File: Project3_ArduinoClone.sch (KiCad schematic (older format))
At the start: 0 parts

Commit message: Added list of parts. Added project symbols, except ATMEGA328. Added child sheet with connectors.
 Changes to be committed:
	new file:   Connectors.sch
	new file:   Portatil/Project3_ArduinoClone-roigmonzon-HP-Pavilion-dv7.pro
	new file:   Portatil/Project3_ArduinoClone-roigmonzon-HP-Pavilion-dv7.sch
	new file:   Project 3 parts.txt
	modified:   Project3_ArduinoClone-cache.lib
	modified:   Project3_ArduinoClone.sch
	modified:   Project3_ArduinoClone.sch-bak
	new file:   instrucciones git.txt
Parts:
- added BT?: Battery, symbol Device:Battery
- added C? (x2): C, symbol Device:C
- added C?: CP, symbol Device:CP
- added D?: LED, symbol Device:LED
- added R? (x2): R, symbol Device:R
- added U?: 24LC1025, symbol Memory_EEPROM:24LC1025
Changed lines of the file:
@@
 EESchema Schematic File Version 4
+LIBS:Project3_ArduinoClone-cache
 EELAYER 30 0
 EELAYER END
 $Descr A4 11693 8268
 encoding utf-8
-Sheet 1 1
+Sheet 1 2
 Title "Arduino Clone"
 Date "2019-10-12"
@@
 Comment4 ""
 $EndDescr
+$Comp
+L Device:Battery BT?
+U 1 1 5DA2ED42
+P 3550 2725
+F 0 "BT?" H 3658 2771 50  0000 L CNN
+F 1 "Battery" H 3658 2680 50  0000 L CNN
+F 2 "" V 3550 2785 50  0001 C CNN
+F 3 "~" V 3550 2785 50  0001 C CNN
+	1    3550 2725
+	1    0    0    -1
+$EndComp
+$Comp
+L Device:C C?
+U 1 1 5DA2FE65
+P 4125 2600
+F 0 "C?" H 4240 2646 50  0000 L CNN
+F 1 "C" H 4240 2555 50  0000 L CNN
+F 2 "" H 4163 2450 50  0001 C CNN
+F 3 "~" H 4125 2600 50  0001 C CNN
+	1    4125 2600
+	1    0    0    -1
+$EndComp
+$Comp
+L Device:C C?
+U 1 1 5DA30297
+P 4125 3075
+F 0 "C?" H 4240 3121 50  0000 L CNN
+F 1 "C" H 4240 3030 50  0000 L CNN
+F 2 "" H 4163 2925 50  0001 C CNN
+F 3 "~" H 4125 3075 50  0001 C CNN
+	1    4125 3075
+	1    0    0    -1
+$EndComp
+$Comp
+L Device:CP C?
+U 1 1 5DA309D4
+P 4125 3650
+F 0 "C?" H 4243 3696 50  0000 L CNN
+F 1 "CP" H 4243 3605 50  0000 L CNN
+F 2 "" H 4163 3500 50  0001 C CNN
+F 3 "~" H 4125 3650 50  0001 C CNN
+	1    4125 3650
+	1    0    0    -1
+$EndComp
+$Comp
+L Device:LED D?
+U 1 1 5DA313E3
+P 3475 3600
+F 0 "D?" H 3468 3816 50  0000 C CNN
+F 1 "LED" H 3468 3725 50  0000 C CNN
+F 2 "" H 3475 3600 50  0001 C CNN
+F 3 "~" H 3475 3600 50  0001 C CNN
+	1    3475 3600
+	1    0    0    -1
+$EndComp
+$Comp
+L Device:R R?
+U 1 1 5DA31FF8
+P 5100 2600
+F 0 "R?" H 5170 2646 50  0000 L CNN
+F 1 "R" H 5170 2555 50  0000 L CNN
+F 2 "" V 5030 2600 50  0001 C CNN
+F 3 "~" H 5100 2600 50  0001 C CNN
+	1    5100 2600
+	1    0    0    -1
+$EndComp
+$Comp
+L Device:R R?
+U 1 1 5DA326D9
+P 5100 3200
+F 0 "R?" H 5170 3246 50  0000 L CNN
+F 1 "R" H 5170 3155 50  0000 L CNN
+F 2 "" V 5030 3200 50  0001 C CNN
+F 3 "~" H 5100 3200 50  0001 C CNN
+	1    5100 3200
+	1    0    0    -1
+$EndComp
+$Comp
+L Memory_EEPROM:24LC1025 U?
+U 1 1 5DA32AA2
+P 6825 2950
+F 0 "U?" H 6825 3431 50  0000 C CNN
+F 1 "24LC1025" H 6825 3340 50  0000 C CNN
+F 2 "" H 6825 2950 50  0001 C CNN
+F 3 "http://ww1.microchip.com/downloads/en/DeviceDoc/21941B.pdf" H 6825 2950 50  0001 C CNN
+	1    6825 2950
+	1    0    0    -1
+$EndComp
+$Sheet
+S 6475 3875 1125 1900
+U 5DA33D85
+F0 "Connectors" 50
+F1 "Connectors.sch" 50
+$EndSheet
 $EndSCHEMATC

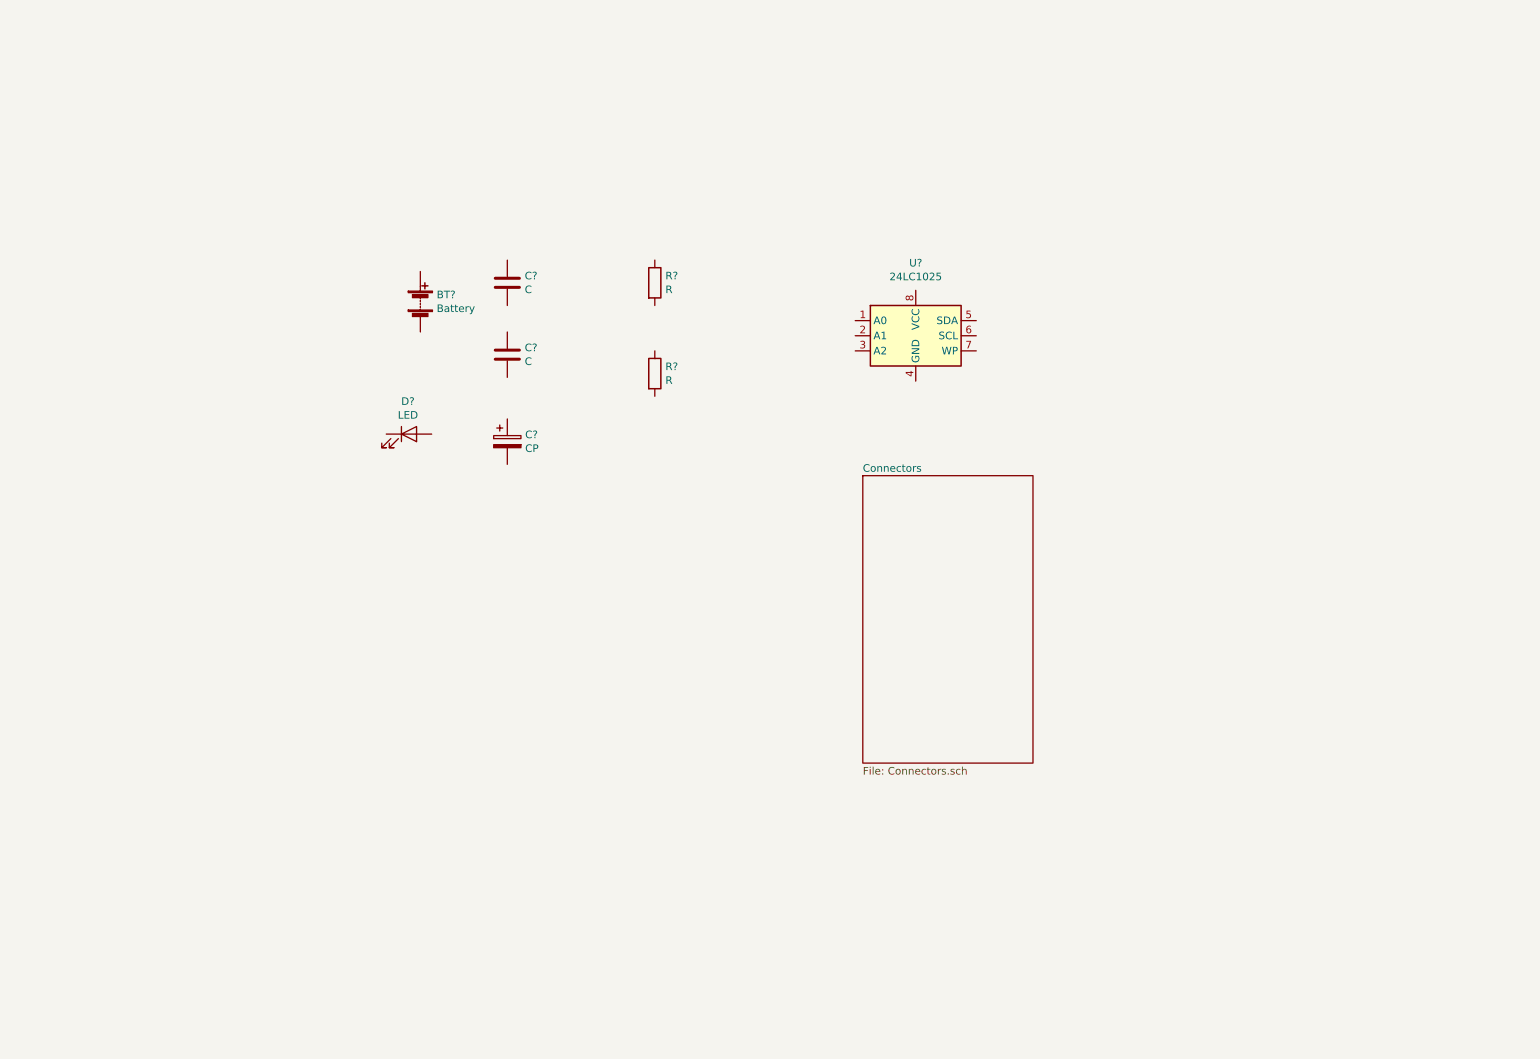
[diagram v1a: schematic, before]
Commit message: Added DS1337 schematic symbol (custom created).
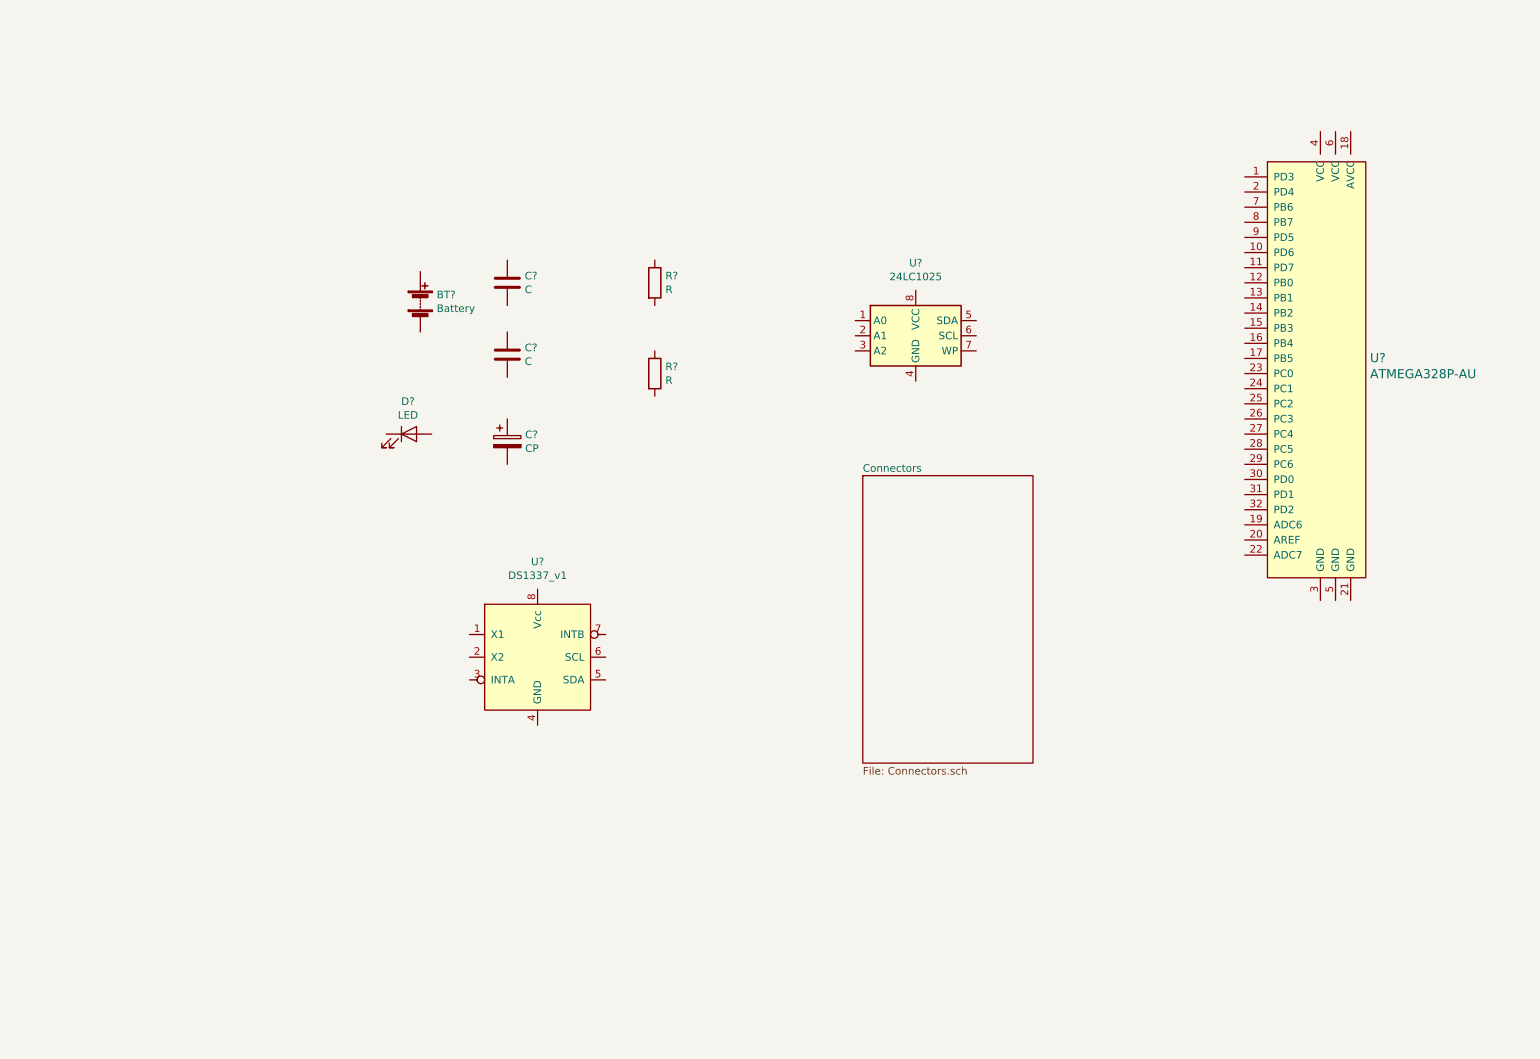
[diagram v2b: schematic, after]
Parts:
- added U?: ATMEGA328P-AU, digikey-footprints:TQFP-32_7x7mm, symbol dk_Embedded-Microcontrollers:ATMEGA328P-AU
- added U?: DS1337_v1, symbol Pablo_KiCad:DS1337_v1
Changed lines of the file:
@@
 F1 "Connectors.sch" 50
 $EndSheet
+$Comp
+L dk_Embedded-Microcontrollers:ATMEGA328P-AU U?
+U 1 1 5DA3240F
+P 9500 3200
+F 0 "U?" H 9828 3303 60  0000 L CNN
+F 1 "ATMEGA328P-AU" H 9828 3197 60  0000 L CNN
+F 2 "digikey-footprints:TQFP-32_7x7mm" H 9700 3400 60  0001 L CNN
+F 3 "http://www.microchip.com/mymicrochip/filehandler.aspx?ddocname=en608326" H 9700 3500 60  0001 L CNN
+F 4 "ATMEGA328P-AU-ND" H 9700 3600 60  0001 L CNN "Digi-Key_PN"
+F 5 "ATMEGA328P-AU" H 9700 3700 60  0001 L CNN "MPN"
+F 6 "Integrated Circuits (ICs)" H 9700 3800 60  0001 L CNN "Category"
+F 7 "Embedded - Microcontrollers" H 9700 3900 60  0001 L CNN "Family"
+F 8 "http://www.microchip.com/mymicrochip/filehandler.aspx?ddocname=en608326" H 9700 4000 60  0001 L CNN "DK_Datasheet_Link"
+F 9 "/product-detail/en/microchip-technology/ATMEGA328P-AU/ATMEGA328P-AU-ND/1832260" H 9700 4100 60  0001 L CNN "DK_Detail_Page"
+F 10 "IC MCU 8BIT 32KB FLASH 32TQFP" H 9700 4200 60  0001 L CNN "Description"
+F 11 "Microchip Technology" H 9700 4300 60  0001 L CNN "Manufacturer"
+F 12 "Active" H 9700 4400 60  0001 L CNN "Status"
+	1    9500 3200
+	1    0    0    -1
+$EndComp
+$Comp
+L Pablo_KiCad:DS1337_v1 U?
+U 1 1 5DA3A1C8
+P 4325 5075
+F 0 "U?" H 4325 5706 50  0000 C CNN
+F 1 "DS1337_v1" H 4325 5615 50  0000 C CNN
+F 2 "" H 4325 5075 50  0001 C CNN
+F 3 "https://datasheets.maximintegrated.com/en/ds/DS1337-DS1337C.pdf" H 4325 5075 50  0001 C CNN
+	1    4325 5075
+	1    0    0    -1
+$EndComp
 $EndSCHEMATC

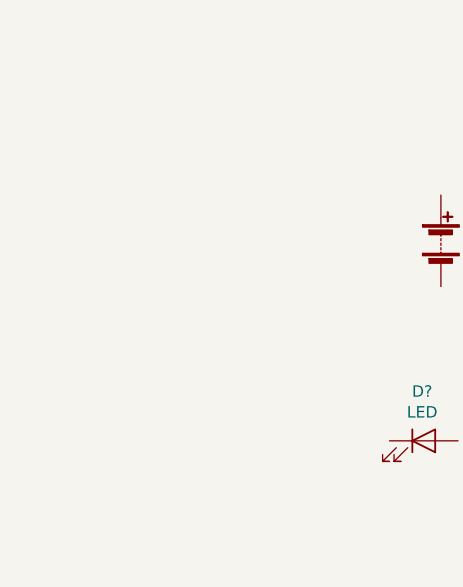
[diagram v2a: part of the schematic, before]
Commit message: Added missing crystals.
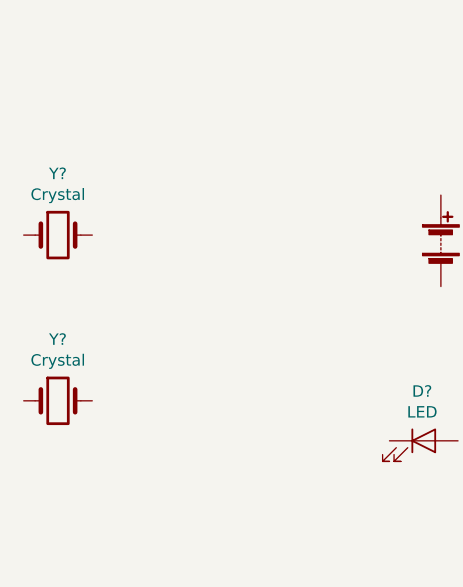
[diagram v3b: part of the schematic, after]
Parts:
- added Y? (x2): Crystal, symbol Device:Crystal
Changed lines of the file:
@@
+	1    0    0    -1
+$EndComp
+$Comp
+L Device:Crystal Y?
+U 1 1 5DA3AECE
+P 1875 2700
+F 0 "Y?" H 1875 2968 50  0000 C CNN
+F 1 "Crystal" H 1875 2877 50  0000 C CNN
+F 2 "" H 1875 2700 50  0001 C CNN
+F 3 "~" H 1875 2700 50  0001 C CNN
+	1    1875 2700
+	1    0    0    -1
+$EndComp
+$Comp
+L Device:Crystal Y?
+U 1 1 5DA3BA19
+P 1875 3425
+F 0 "Y?" H 1875 3693 50  0000 C CNN
+F 1 "Crystal" H 1875 3602 50  0000 C CNN
+F 2 "" H 1875 3425 50  0001 C CNN
+F 3 "~" H 1875 3425 50  0001 C CNN
+	1    1875 3425
 	1    0    0    -1
 $EndComp

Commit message: Annotated.
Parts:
- added U2: 24LC1025, symbol Memory_EEPROM:24LC1025
- gave numbers to parts that had none: 12
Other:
- moved on the sheet: BT1, C1, C2, C3, D1, R1, R2, U1, U3, U4, Y1, Y2
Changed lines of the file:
@@
 $EndDescr
 $Comp
-L Device:Battery BT?
+L Device:Battery BT1
 U 1 1 5DA2ED42
-P 3550 2725
-F 0 "BT?" H 3658 2771 50  0000 L CNN
-F 1 "Battery" H 3658 2680 50  0000 L CNN
-F 2 "" V 3550 2785 50  0001 C CNN
-F 3 "~" V 3550 2785 50  0001 C CNN
-	1    3550 2725
+P 9450 2975
+F 0 "BT1" H 9558 3021 50  0000 L CNN
+F 1 "Battery" H 9558 2930 50  0000 L CNN
+F 2 "" V 9450 3035 50  0001 C CNN
+F 3 "~" V 9450 3035 50  0001 C CNN
+	1    9450 2975
 	1    0    0    -1
 $EndComp
 $Comp
-L Device:C C?
+L Device:C C1
 U 1 1 5DA2FE65
-P 4125 2600
-F 0 "C?" H 4240 2646 50  0000 L CNN
-F 1 "C" H 4240 2555 50  0000 L CNN
-F 2 "" H 4163 2450 50  0001 C CNN
-F 3 "~" H 4125 2600 50  0001 C CNN
-	1    4125 2600
+P 4725 2425
+F 0 "C1" H 4840 2471 50  0000 L CNN
+F 1 "C" H 4840 2380 50  0000 L CNN
+F 2 "" H 4763 2275 50  0001 C CNN
+F 3 "~" H 4725 2425 50  0001 C CNN
+	1    4725 2425
 	1    0    0    -1
 $EndComp
 $Comp
-L Device:C C?
+L Device:C C2
 U 1 1 5DA30297
-P 4125 3075
-F 0 "C?" H 4240 3121 50  0000 L CNN
-F 1 "C" H 4240 3030 50  0000 L CNN
-F 2 "" H 4163 2925 50  0001 C CNN
-F 3 "~" H 4125 3075 50  0001 C CNN
-	1    4125 3075
+P 4725 2900
+F 0 "C2" H 4840 2946 50  0000 L CNN
+F 1 "C" H 4840 2855 50  0000 L CNN
+F 2 "" H 4763 2750 50  0001 C CNN
+F 3 "~" H 4725 2900 50  0001 C CNN
+	1    4725 2900
 	1    0    0    -1
 $EndComp
 $Comp
-L Device:CP C?
+L Device:CP C3
 U 1 1 5DA309D4
-P 4125 3650
-F 0 "C?" H 4243 3696 50  0000 L CNN
-F 1 "CP" H 4243 3605 50  0000 L CNN
-F 2 "" H 4163 3500 50  0001 C CNN
-F 3 "~" H 4125 3650 50  0001 C CNN
-	1    4125 3650
+P 10025 3900
+F 0 "C3" H 10143 3946 50  0000 L CNN
+F 1 "CP" H 10143 3855 50  0000 L CNN
+F 2 "" H 10063 3750 50  0001 C CNN
+F 3 "~" H 10025 3900 50  0001 C CNN
+	1    10025 3900
 	1    0    0    -1
 $EndComp
 $Comp
-L Device:LED D?
+L Device:LED D1
 U 1 1 5DA313E3
-P 3475 3600
-F 0 "D?" H 3468 3816 50  0000 C CNN
-F 1 "LED" H 3468 3725 50  0000 C CNN
-F 2 "" H 3475 3600 50  0001 C CNN
-F 3 "~" H 3475 3600 50  0001 C CNN
-	1    3475 3600
+P 5475 3575
+F 0 "D1" H 5468 3791 50  0000 C CNN
+F 1 "LED" H 5468 3700 50  0000 C CNN
+F 2 "" H 5475 3575 50  0001 C CNN
+F 3 "~" H 5475 3575 50  0001 C CNN
+	1    5475 3575
 	1    0    0    -1
 $EndComp
 $Comp
-L Device:R R?
+L Device:R R1
 U 1 1 5DA31FF8
-P 5100 2600
-F 0 "R?" H 5170 2646 50  0000 L CNN
-F 1 "R" H 5170 2555 50  0000 L CNN
-F 2 "" V 5030 2600 50  0001 C CNN
-F 3 "~" H 5100 2600 50  0001 C CNN
-	1    5100 2600
+P 4950 3800
+F 0 "R1" H 5020 3846 50  0000 L CNN
+F 1 "R" H 5020 3755 50  0000 L CNN
+F 2 "" V 4880 3800 50  0001 C CNN
+F 3 "~" H 4950 3800 50  0001 C CNN
+	1    4950 3800
 	1    0    0    -1
 $EndComp
 $Comp
-L Device:R R?
+L Device:R R2
 U 1 1 5DA326D9
-P 5100 3200
-F 0 "R?" H 5170 3246 50  0000 L CNN
-F 1 "R" H 5170 3155 50  0000 L CNN
-F 2 "" V 5030 3200 50  0001 C CNN
-F 3 "~" H 5100 3200 50  0001 C CNN
-	1    5100 3200
+P 5625 4600
+F 0 "R2" H 5695 4646 50  0000 L CNN
+F 1 "R" H 5695 4555 50  0000 L CNN
+F 2 "" V 5555 4600 50  0001 C CNN
+F 3 "~" H 5625 4600 50  0001 C CNN
+	1    5625 4600
 	1    0    0    -1
 $EndComp
 $Comp
-L Memory_EEPROM:24LC1025 U?
+L Memory_EEPROM:24LC1025 U1
 U 1 1 5DA32AA2
-P 6825 2950
-F 0 "U?" H 6825 3431 50  0000 C CNN
-F 1 "24LC1025" H 6825 3340 50  0000 C CNN
-F 2 "" H 6825 2950 50  0001 C CNN
-F 3 "http://ww1.microchip.com/downloads/en/DeviceDoc/21941B.pdf" H 6825 2950 50  0001 C CNN
-	1    6825 2950
+P 1825 4450
+F 0 "U1" H 1825 4931 50  0000 C CNN
+F 1 "24LC1025" H 1825 4840 50  0000 C CNN
+F 2 "" H 1825 4450 50  0001 C CNN
+F 3 "http://ww1.microchip.com/downloads/en/DeviceDoc/21941B.pdf" H 1825 4450 50  0001 C CNN
+	1    1825 4450
 	1    0    0    -1
 $EndComp
 $Sheet
-S 6475 3875 1125 1900
+S 3075 5075 1125 1900
 U 5DA33D85
 F0 "Connectors" 50
@@
 $EndSheet
 $Comp
-L dk_Embedded-Microcontrollers:ATMEGA328P-AU U?
+L dk_Embedded-Microcontrollers:ATMEGA328P-AU U4
 U 1 1 5DA3240F
-P 9500 3200
-F 0 "U?" H 9828 3303 60  0000 L CNN
-F 1 "ATMEGA328P-AU" H 9828 3197 60  0000 L CNN
-F 2 "digikey-footprints:TQFP-32_7x7mm" H 9700 3400 60  0001 L CNN
-F 3 "http://www.microchip.com/mymicrochip/filehandler.aspx?ddocname=en608326" H 9700 3500 60  0001 L CNN
-F 4 "ATMEGA328P-AU-ND" H 9700 3600 60  0001 L CNN "Digi-Key_PN"
-F 5 "ATMEGA328P-AU" H 9700 3700 60  0001 L CNN "MPN"
-F 6 "Integrated Circuits (ICs)" H 9700 3800 60  0001 L CNN "Category"
-F 7 "Embedded - Microcontrollers" H 9700 3900 60  0001 L CNN "Family"
-F 8 "http://www.microchip.com/mymicrochip/filehandler.aspx?ddocname=en608326" H 9700 4000 60  0001 L CNN "DK_Datasheet_Link"
-F 9 "/product-detail/en/microchip-technology/ATMEGA328P-AU/ATMEGA328P-AU-ND/1832260" H 9700 4100 60  0001 L CNN "DK_Detail_Page"
-F 10 "IC MCU 8BIT 32KB FLASH 32TQFP" H 9700 4200 60  0001 L CNN "Description"
-F 11 "Microchip Technology" H 9700 4300 60  0001 L CNN "Manufacturer"
-F 12 "Active" H 9700 4400 60  0001 L CNN "Status"
-	1    9500 3200
+P 7100 3575
+F 0 "U4" H 7428 3678 60  0000 L CNN
+F 1 "ATMEGA328P-AU" H 7428 3572 60  0000 L CNN
+F 2 "digikey-footprints:TQFP-32_7x7mm" H 7300 3775 60  0001 L CNN
+F 3 "http://www.microchip.com/mymicrochip/filehandler.aspx?ddocname=en608326" H 7300 3875 60  0001 L CNN
+F 4 "ATMEGA328P-AU-ND" H 7300 3975 60  0001 L CNN "Digi-Key_PN"
+F 5 "ATMEGA328P-AU" H 7300 4075 60  0001 L CNN "MPN"
+F 6 "Integrated Circuits (ICs)" H 7300 4175 60  0001 L CNN "Category"
+F 7 "Embedded - Microcontrollers" H 7300 4275 60  0001 L CNN "Family"
+F 8 "http://www.microchip.com/mymicrochip/filehandler.aspx?ddocname=en608326" H 7300 4375 60  0001 L CNN "DK_Datasheet_Link"
+F 9 "/product-detail/en/microchip-technology/ATMEGA328P-AU/ATMEGA328P-AU-ND/1832260" H 7300 4475 60  0001 L CNN "DK_Detail_Page"
+F 10 "IC MCU 8BIT 32KB FLASH 32TQFP" H 7300 4575 60  0001 L CNN "Description"
+F 11 "Microchip Technology" H 7300 4675 60  0001 L CNN "Manufacturer"
+F 12 "Active" H 7300 4775 60  0001 L CNN "Status"
+	1    7100 3575
 	1    0    0    -1
 $EndComp
 $Comp
-L Pablo_KiCad:DS1337_v1 U?
+L Pablo_KiCad:DS1337_v1 U3
 U 1 1 5DA3A1C8
-P 4325 5075
-F 0 "U?" H 4325 5706 50  0000 C CNN
-F 1 "DS1337_v1" H 4325 5615 50  0000 C CNN
-F 2 "" H 4325 5075 50  0001 C CNN
-F 3 "https://datasheets.maximintegrated.com/en/ds/DS1337-DS1337C.pdf" H 4325 5075 50  0001 C CNN
-	1    4325 5075
+P 2625 1850
+F 0 "U3" H 2625 2481 50  0000 C CNN
+F 1 "DS1337_v1" H 2625 2390 50  0000 C CNN
+F 2 "" H 2625 1850 50  0001 C CNN
+F 3 "https://datasheets.maximintegrated.com/en/ds/DS1337-DS1337C.pdf" H 2625 1850 50  0001 C CNN
+	1    2625 1850
 	1    0    0    -1
 $EndComp
 $Comp
-L Device:Crystal Y?
+L Device:Crystal Y1
 U 1 1 5DA3AECE
-P 1875 2700
-F 0 "Y?" H 1875 2968 50  0000 C CNN
-F 1 "Crystal" H 1875 2877 50  0000 C CNN
-F 2 "" H 1875 2700 50  0001 C CNN
-F 3 "~" H 1875 2700 50  0001 C CNN
-	1    1875 2700
+P 1600 1750
+F 0 "Y1" V 1554 1881 50  0000 L CNN
+F 1 "Crystal" V 1645 1881 50  0000 L CNN
+F 2 "" H 1600 1750 50  0001 C CNN
+F 3 "~" H 1600 1750 50  0001 C CNN
+	1    1600 1750
+	0    1    1    0
+$EndComp
+$Comp
+L Device:Crystal Y2
+U 1 1 5DA3BA19
+P 5300 2650
+F 0 "Y2" V 5254 2781 50  0000 L CNN
+F 1 "Crystal" V 5345 2781 50  0000 L CNN
+F 2 "" H 5300 2650 50  0001 C CNN
+F 3 "~" H 5300 2650 50  0001 C CNN
+	1    5300 2650
+	0    1    1    0
+$EndComp
+$Comp
+L Memory_EEPROM:24LC1025 U2
+U 1 1 5DA3CEF9
+P 1825 5325
+F 0 "U2" H 1825 5806 50  0000 C CNN
+F 1 "24LC1025" H 1825 5715 50  0000 C CNN
+F 2 "" H 1825 5325 50  0001 C CNN
+F 3 "http://ww1.microchip.com/downloads/en/DeviceDoc/21941B.pdf" H 1825 5325 50  0001 C CNN
+	1    1825 5325
 	1    0    0    -1
 $EndComp
 $Comp
-L Device:Crystal Y?
-U 1 1 5DA3BA19
-P 1875 3425
-F 0 "Y?" H 1875 3693 50  0000 C CNN
-F 1 "Crystal" H 1875 3602 50  0000 C CNN
-F 2 "" H 1875 3425 50  0001 C CNN
-F 3 "~" H 1875 3425 50  0001 C CNN
-	1    1875 3425
+L power:GND #PWR01
+U 1 1 5DA4B133
+P 9550 4225
+F 0 "#PWR01" H 9550 3975 50  0001 C CNN
+F 1 "GND" H 9555 4052 50  0000 C CNN
+F 2 "" H 9550 4225 50  0001 C CNN
+F 3 "" H 9550 4225 50  0001 C CNN
+	1    9550 4225
 	1    0    0    -1
 $EndComp
